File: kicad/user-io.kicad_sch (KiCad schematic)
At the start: 45 parts, among them J1 Lower Bank, J2 Upper Bank, SW1 PTS815, U1 MIMXRT1171DVMAB, U2 MAYA-W166-00B, U3 LSM6DSV, U4 LIS2MDL, U5 RTMC-G2-4IQ48, Y1 8MHz

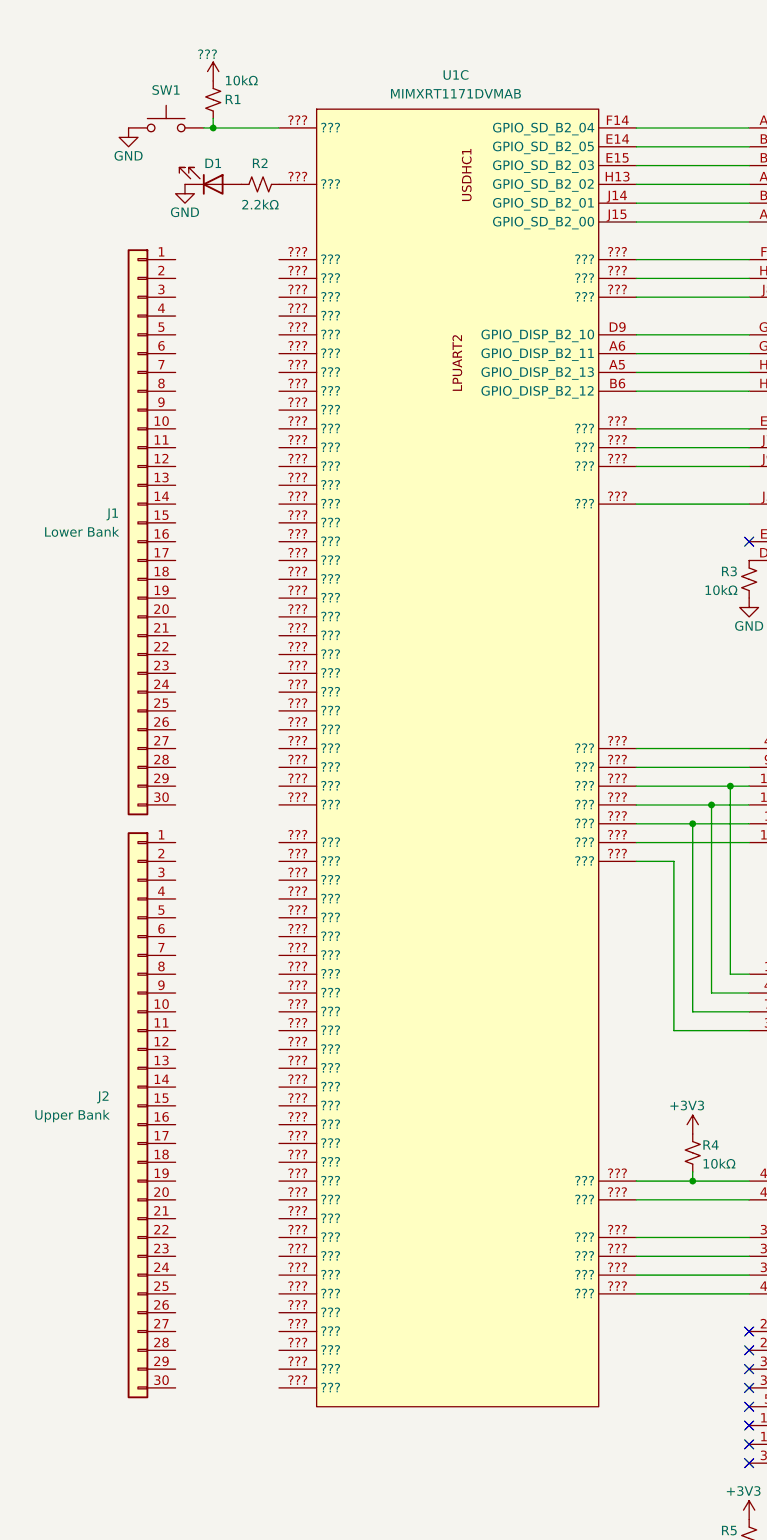
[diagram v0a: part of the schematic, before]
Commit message: finished preliminary routing
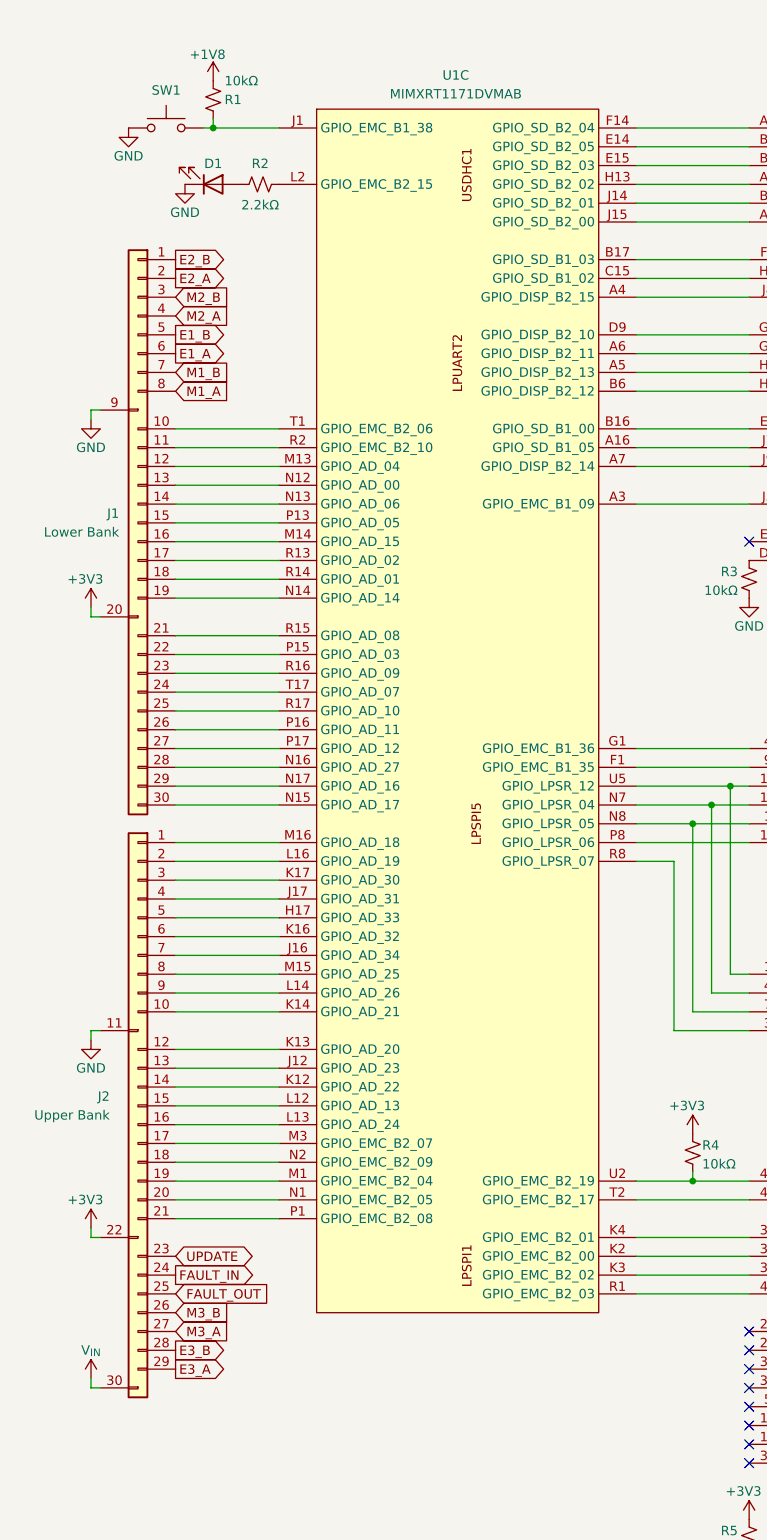
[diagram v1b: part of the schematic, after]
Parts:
- J1: symbol Connector_Generic:Conn_01x30 -> project_symbols:IO_Bank_Lower
- J2: symbol Connector_Generic:Conn_01x30 -> project_symbols:IO_Bank_Upper
- U1: footprint Package_BGA:MAPBGA-289_14x14mm_Layout17x17_P0.8mm -> project_footprints:MIMXRT1171DVMAB
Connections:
- net ??? is gone; now on net +1V8: R1.2
- net +3V3: now also J1.20 (Pin_20), J2.22 (Pin_22)
- net E1_A: now also J1.6 (Pin_6)
- net E1_B: now also J1.5 (Pin_5)
- net E2_A: now also J1.2 (Pin_2)
- net E2_B: now also J1.1 (Pin_1)
- net E3_A: now also J2.29 (Pin_29)
- net E3_B: now also J2.28 (Pin_28)
- net FAULT_IN: now also J2.24 (Pin_24)
- net FAULT_OUT: now also J2.25 (Pin_25)
- net GND: now also J1.9 (Pin_9), J2.11 (Pin_11)
- net M1_A: now also J1.8 (Pin_8)
- net M1_B: now also J1.7 (Pin_7)
- net M2_A: now also J1.4 (Pin_4)
- net M2_B: now also J1.3 (Pin_3)
- net M3_A: now also J2.27 (Pin_27)
- net M3_B: now also J2.26 (Pin_26)
- net UPDATE: now also J2.23 (Pin_23)
- net at U5.37 (CS_N): now also U1.K4 (GPIO_EMC_B2_01); no longer U1.???
- net at U5.38 (SCLK): now also U1.K2 (GPIO_EMC_B2_00); no longer U1.???
- net at U5.39 (DI): now also U1.K3 (GPIO_EMC_B2_02); no longer U1.???
- net at U5.40 (DO): now also U1.R1 (GPIO_EMC_B2_03); no longer U1.???
- net at U5.47 (INTER): now also U1.T2 (GPIO_EMC_B2_17); no longer U1.???
- net at R4.2, U5.48 (RESET_N): now also U1.U2 (GPIO_EMC_B2_19); no longer U1.???
- net at U3.1 (SDO), U4.7 (SDO): now also U1.N8 (GPIO_LPSR_05); no longer U1.???
- net at U3.12 (CS): now also U1.P8 (GPIO_LPSR_06); no longer U1.???
- net at U3.13 (SCL), U4.1 (SPC): now also U1.U5 (GPIO_LPSR_12); no longer U1.???
- net at U3.14 (SDI), U4.4 (SDI): now also U1.N7 (GPIO_LPSR_04); no longer U1.???
- net at U3.4 (INT1): now also U1.G1 (GPIO_EMC_B1_36); no longer U1.???
- net at U3.9 (INT2): now also U1.F1 (GPIO_EMC_B1_35); no longer U1.???
- net at J1.10 (Pin_10): now also U1.T1 (GPIO_EMC_B2_06)
- net at J1.11 (Pin_11): now also U1.R2 (GPIO_EMC_B2_10)
- net at J1.12 (Pin_12): now also U1.M13 (GPIO_AD_04)
- net at J1.13 (Pin_13): now also U1.N12 (GPIO_AD_00)
- net at J1.14 (Pin_14): now also U1.N13 (GPIO_AD_06)
- net at J1.15 (Pin_15): now also U1.P13 (GPIO_AD_05)
- net at J1.16 (Pin_16): now also U1.M14 (GPIO_AD_15)
- net at J1.17 (Pin_17): now also U1.R13 (GPIO_AD_02)
- net at J1.18 (Pin_18): now also U1.R14 (GPIO_AD_01)
- net at J1.19 (Pin_19): now also U1.N14 (GPIO_AD_14)
- net at J1.21 (Pin_21): now also U1.R15 (GPIO_AD_08)
- net at J1.22 (Pin_22): now also U1.P15 (GPIO_AD_03)
- net at J1.23 (Pin_23): now also U1.R16 (GPIO_AD_09)
- net at J1.24 (Pin_24): now also U1.T17 (GPIO_AD_07)
- net at J1.25 (Pin_25): now also U1.R17 (GPIO_AD_10)
- net at J1.26 (Pin_26): now also U1.P16 (GPIO_AD_11)
- net at J1.27 (Pin_27): now also U1.P17 (GPIO_AD_12)
- net at J1.28 (Pin_28): now also U1.N16 (GPIO_AD_27)
- net at J1.29 (Pin_29): now also U1.N17 (GPIO_AD_16)
- net at J1.30 (Pin_30): now also U1.N15 (GPIO_AD_17)
- net at U4.3 (CS): now also U1.R8 (GPIO_LPSR_07); no longer U1.???
- net at R1.1, SW1.2: now also U1.J1 (GPIO_EMC_B1_38); no longer U1.???
- net at R2.2: now also U1.L2 (GPIO_EMC_B2_15); no longer U1.???
- net at U2.E7 (BT_WAKE_HOST): now also U1.B16 (GPIO_SD_B1_00); no longer U1.???
- net at U2.F7 (WLAN_WAKE_HOST): now also U1.B17 (GPIO_SD_B1_03); no longer U1.???
- net at U2.H7 (WLAN_RESET): now also U1.C15 (GPIO_SD_B1_02); no longer U1.???
- net at U2.J3 (PDn): now also U1.A3 (GPIO_EMC_B1_09); no longer U1.???
- net at U2.J7 (BT_RESET): now also U1.A16 (GPIO_SD_B1_05); no longer U1.???
- net at U2.J8 (WLAN_DEV_WAKE): now also U1.A4 (GPIO_DISP_B2_15); no longer U1.???
- net at U2.J9 (BT_DEV_WAKE): now also U1.A7 (GPIO_DISP_B2_14); no longer U1.???
- net at J2.1 (Pin_1): now also U1.M16 (GPIO_AD_18)
- net at J2.10 (Pin_10): now also U1.K14 (GPIO_AD_21)
- net at J2.12 (Pin_12): now also U1.K13 (GPIO_AD_20)
- net at J2.13 (Pin_13): now also U1.J12 (GPIO_AD_23)
- net at J2.14 (Pin_14): now also U1.K12 (GPIO_AD_22)
- net at J2.15 (Pin_15): now also U1.L12 (GPIO_AD_13)
- net at J2.16 (Pin_16): now also U1.L13 (GPIO_AD_24)
- net at J2.17 (Pin_17): now also U1.M3 (GPIO_EMC_B2_07)
- net at J2.18 (Pin_18): now also U1.N2 (GPIO_EMC_B2_09)
- net at J2.19 (Pin_19): now also U1.M1 (GPIO_EMC_B2_04)
- net at J2.2 (Pin_2): now also U1.L16 (GPIO_AD_19)
- net at J2.20 (Pin_20): now also U1.N1 (GPIO_EMC_B2_05)
- net at J2.21 (Pin_21): now also U1.P1 (GPIO_EMC_B2_08)
- net at J2.3 (Pin_3): now also U1.K17 (GPIO_AD_30)
- net V_{IN}: now reaches J2.30 (Pin_30)
- net at J2.4 (Pin_4): now also U1.J17 (GPIO_AD_31)
- net at J2.5 (Pin_5): now also U1.H17 (GPIO_AD_33)
- net at J2.6 (Pin_6): now also U1.K16 (GPIO_AD_32)
- net at J2.7 (Pin_7): now also U1.J16 (GPIO_AD_34)
- net at J2.8 (Pin_8): now also U1.M15 (GPIO_AD_25)
- net at J2.9 (Pin_9): now also U1.L14 (GPIO_AD_26)
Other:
- moved on the sheet: J1, J2
